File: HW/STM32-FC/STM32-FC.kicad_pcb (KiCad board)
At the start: 4 copper layers, 38 x 48 mm, 113 parts, among them J1 GH 1.25mm 6P, J10 GH 1.25mm 6P, J11 GH 1.25mm 6P, J12 GH 1.25mm 6P, J13 GH 1.25mm 4P, J14 GH 1.25mm 4P, J15 GH 1.25mm 4P, J2 USB_C_USB2.0_14P, J3 GH 1.25mm 6P, J4 Micro_SD_Card_Det1, J5 JST ZH 1.5mm 2P, J6 PWM_Conn_3x14, J7 ZH 1.5mm 3P, J8 ZH 1.5mm 4P, J9 GH 1.25mm 10P, Q1 S9013, Q2 S9013, SW2 SW_DIP_x03, U1 STM32F407VETx, U10 ATA6561-GBQW, U11 ATA6561-GBQW, U2 USBLC6-2SC6, U3 AMS1117-3.3, U4 AMS1117-3.3, U5 W25X40CLSN, U6 BMI323, U7 ICM-42688-P, U8 LIS2MDLTR, U9 LPS22HH, Y1 16MHz

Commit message: 2025.02.05 PCB routing 3
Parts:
- R17: value 10k -> 15k
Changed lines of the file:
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@@
 			)
 		)
-		(property "Value" "10k"
+		(property "Value" "15k"
 			(at 0 1.17 90)
 			(layer "F.Fab")
@@
 		(tags "Through hole pin header THT 1x03 1.27mm single row")
 		(property "Reference" "TP2"
-			(at 0 1.695 360)
+			(at 0 1.695 0)
 			(layer "B.SilkS")
 			(hide yes)
@@
 		)
 		(property "Value" "Test Pin"
-			(at 0 -4.235 360)
+			(at 0 -4.235 0)
 			(layer "B.Fab")
 			(effects
@@
 		)
 		(fp_text user "${REFERENCE}"
-			(at 1.85 0 360)
+			(at 1.85 0 0)
 			(layer "B.Fab")
 			(effects

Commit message: 2025.02.05 PCB routing done
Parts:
- removed R35: 0, Resistor_SMD:R_0402_1005Metric
- added JP1: SolderJumper_2_Open, Jumper:SolderJumper-2_P1.3mm_Open_TrianglePad1.0x1.5mm, F.Cu at (123.5, 116.4)
- moved R29 0.86 mm to (151.9, 78.9), turned to 0 degrees
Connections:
- J6 pad 2: /TIM4_CH4 -> /TIM3_CH1
- J6 pad 3: /TIM3_CH1 -> /TIM3_CH2
- J6 pad 4: /TIM3_CH2 -> /TIM4_CH4
- U1 pad 15: /RSSI_IN -> /V_BATT
- U1 pad 16: /V_BATT -> /RSSI_IN
- U1 pad 39: /GPS1_LED -> unconnected-(U1-PE8-Pad39)
- U1 pad 40: /GPS1_BUZZER -> unconnected-(U1-PE9-Pad40)
- U1 pad 41: /GPS1_LED_SW -> unconnected-(U1-PE10-Pad41)
- U1 pad 57: unconnected-(U1-PD10-Pad57) -> /GPS1_LED_SW
- U1 pad 60: unconnected-(U1-PD13-Pad60) -> /GPS1_LED
- U1 pad 65: unconnected-(U1-PC8-Pad65) -> /GPS1_BUZZER
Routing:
- net /UART5_TX: track 0.00 -> 63.7 mm, vias 0 -> 2
- net /UART5_RX: track 2.22 -> 60.2 mm, vias 0 -> 2
- net +3.3V_RC: track 10.9 -> 54.9 mm, vias 0 -> 3
- net /TIM3_CH1: track 0.00 -> 39.3 mm, vias 0 -> 1
- net /TIM3_CH2: track 0.00 -> 37.5 mm, vias 0 -> 1
- net /TIM4_CH4: track 0.00 -> 36.6 mm, vias 0 -> 1
- net /TIM1_CH4: track 17.8 -> 52.3 mm, vias 0 -> 2
- net /I2C1_SCL: track 2.22 -> 34.6 mm, vias 0 -> 2
- net /I2C1_SDA: track 3.95 -> 35.9 mm, vias 0 -> 2
- net /TIM1_CH3: track 0.00 -> 31.3 mm, vias 0 -> 2
- net /MSD_DETECT: track 0.00 -> 28.3 mm, vias 0 -> 2
- net /CAN2_STBY: track 0.00 -> 27.6 mm, vias 0 -> 3
- net /TIM1_CH2: track 0.00 -> 23.9 mm, vias 0 -> 1
- net /TIM3_CH3: track 0.00 -> 23.1 mm, vias 0 -> 1
- net /CAN1_STBY: track 0.00 -> 23.0 mm, vias 0 -> 1
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
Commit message: 2025.02.06 PCB routing done v2
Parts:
- added C35: 100nF, Capacitor_SMD:C_0402_1005Metric, F.Cu at (134.1, 97.8)
- D1, D2, D4, D5, R4, R6, R7, R8: moved to F.Cu
- moved R30 5.38 mm to (138.4, 76.4), turned to 180 degrees
- moved R26 5.00 mm to (131.0, 76.8), turned to 0 degrees
- moved R25 3.81 mm to (126.8, 100.3)
- moved R28 1.61 mm to (126.8, 97.9)
- moved R24 1.50 mm to (129.0, 77.0)
- moved R23 1.40 mm to (127.6, 77.0)
- moved R31 1.32 mm to (126.8, 99.0)
- moved R32 1.22 mm to (126.8, 100.2)
- moved R27 1.17 mm to (126.8, 99.2)
- moved D1 0.50 mm to (146.2, 104.2)
- moved D2 0.50 mm to (146.2, 101.2)
- moved D4 0.50 mm to (146.2, 102.2)
- moved D5 0.50 mm to (146.2, 103.2)
- moved R4 0.50 mm to (148.2, 104.2)
- moved R6 0.50 mm to (148.2, 101.2)
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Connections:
- J1 pad 1: +3.3V -> GND
- J1 pad 2: /SWDIO -> unconnected-(J1-Pin_2-Pad2)
- J1 pad 3: /SWCLK -> /NRST
- J1 pad 4: /NRST -> /SWCLK
- J1 pad 5: unconnected-(J1-Pin_5-Pad5) -> /SWDIO
- J1 pad 6: GND -> +3.3V
- J10 pad 1: +5V -> GND
- J10 pad 2: /UART5_TX -> /I2C2_SDA
- J10 pad 3: /UART5_RX -> /I2C2_SCL
- J10 pad 4: /I2C2_SCL -> /UART5_RX
- J10 pad 5: /I2C2_SDA -> /UART5_TX
- J10 pad 6: GND -> +5V
- J11 pad 1: +5V -> GND
- J11 pad 2: /UART2_TX -> /UART2_RTS
- J11 pad 3: /UART2_RX -> /UART2_CTS
- J11 pad 4: /UART2_CTS -> /UART2_RX
- J11 pad 5: /UART2_RTS -> /UART2_TX
- J11 pad 6: GND -> +5V
- J12 pad 1: +5V -> GND
- J12 pad 2: /UART3_TX -> /UART3_RTS
- J12 pad 3: /UART3_RX -> /UART3_CTS
- J12 pad 4: /UART3_CTS -> /UART3_RX
- J12 pad 5: /UART3_RTS -> /UART3_TX
- J12 pad 6: GND -> +5V
- J13 pad 1: +5V -> GND
- J13 pad 2: /I2C1_SCL -> /I2C1_SDA
- J13 pad 3: /I2C1_SDA -> /I2C1_SCL
- J13 pad 4: GND -> +5V
- J14 pad 1: +5V -> GND
- J14 pad 2: /Communication/CAN1_P -> /Communication/CAN1_N
- J14 pad 3: /Communication/CAN1_N -> /Communication/CAN1_P
- J14 pad 4: GND -> +5V
- J15 pad 1: +5V -> GND
- J15 pad 2: /Communication/CAN2_P -> /Communication/CAN2_N
- J15 pad 3: /Communication/CAN2_N -> /Communication/CAN2_P
- J15 pad 4: GND -> +5V
- J3 pad 1: +5V -> GND
- J3 pad 2: +5V -> GND
- J3 pad 3: /PM_CURRENT -> /PM_VOLTAGE
- J3 pad 4: /PM_VOLTAGE -> /PM_CURRENT
- J3 pad 5: GND -> +5V
- J3 pad 6: GND -> +5V
- J9 pad 1: +5V -> GND
- J9 pad 10: GND -> +5V
- J9 pad 2: /UART4_TX -> /GPS1_BUZZER
- J9 pad 3: /UART4_RX -> +3.3V
- J9 pad 4: /I2C3_SCL -> /GPS1_SW_LED
- J9 pad 5: /I2C3_SDA -> /GPS1_SW
- J9 pad 6: /GPS1_LED_SW -> /I2C3_SDA
- J9 pad 7: /GPS1_LED -> /I2C3_SCL
- J9 pad 8: +3.3V -> /UART4_RX
- J9 pad 9: /GPS1_BUZZER -> /UART4_TX
- U1 pad 37: unconnected-(U1-PB2-Pad37) -> /BOOT1
- U1 pad 57: /GPS1_LED_SW -> /GPS1_SW_LED
- U1 pad 60: /GPS1_LED -> /GPS1_SW
- U1 pad 77: /BOOT1 -> unconnected-(U1-PA15-Pad77)
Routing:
- net /GPS1_SW: track 0.00 -> 17.9 mm, vias 0 -> 2
- net /GPS1_SW_LED: track 0.00 -> 16.9 mm, vias 0 -> 2
- net +3.3V: track 113.1 -> 128.9 mm, vias 23 -> 25
- net /BOOT1: track 21.3 -> 35.5 mm
- net /GPS1_LED: track 14.1 -> 0.00 mm, vias 1 -> 0
- net /GPS1_LED_SW: track 13.5 -> 0.00 mm, vias 1 -> 0
- net /GPS1_BUZZER: track 10.7 -> 20.7 mm, vias 1 -> 2
- net /Communication/CAN1_N: track 6.02 -> 15.4 mm
- net /UART3_RX: track 22.9 -> 13.6 mm
- net /Communication/CAN1_P: track 6.02 -> 14.1 mm
- net GND: track 167.0 -> 174.4 mm, vias 26 -> 39
- net /I2C3_SDA: track 18.0 -> 24.6 mm
- net /I2C3_SCL: track 27.1 -> 20.8 mm
- net /UART4_TX: track 27.3 -> 21.3 mm
- net /UART4_RX: track 27.6 -> 21.9 mm
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
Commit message: 2025.02.06 PCB routing done v3
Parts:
- J1, J10, J11, J12, J3: footprint JST_GH:JST_GH_BM06B-GHS-TBT_06 -> JST_GH:JST_GH_SM06B-GHS-TB_06x1.25mm_Angled
- J13, J14, J15: footprint JST_GH:JST_GH_BM04B-GHS-TBT_04 -> JST_GH:JST_GH_SM04B-GHS-TB_04x1.25mm_Angled
- J9: footprint JST_GH:JST_GH_BM10B-GHS-TBT_10 -> JST_GH:JST_GH_SM10B-GHS-TB_10x1.25mm_Angled
- turned J1 to 90 degrees
- turned J10 to -90 degrees
- turned J11 to 0 degrees
- turned J12 to 0 degrees
- turned J13 to 90 degrees
- turned J14 to 180 degrees
- turned J15 to 180 degrees
- turned J3 to 0 degrees
- turned J9 to 180 degrees
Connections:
- net /TIM4_CH3 renamed /Buzzer
- J1 pad 1: GND -> +3.3V
- J1 pad 2: unconnected-(J1-Pin_2-Pad2) -> /SWDIO
- J1 pad 3: /NRST -> /SWCLK
- J1 pad 4: /SWCLK -> /NRST
- J1 pad 5: /SWDIO -> unconnected-(J1-Pin_5-Pad5)
- J1 pad 6: +3.3V -> GND
- J10 pad 1: GND -> +5V
- J10 pad 2: /I2C2_SDA -> /UART5_TX
- J10 pad 3: /I2C2_SCL -> /UART5_RX
- J10 pad 4: /UART5_RX -> /I2C2_SCL
- J10 pad 5: /UART5_TX -> /I2C2_SDA
- J10 pad 6: +5V -> GND
- J11 pad 1: GND -> +5V
- J11 pad 2: /UART2_RTS -> /UART2_TX
- J11 pad 3: /UART2_CTS -> /UART2_RX
- J11 pad 4: /UART2_RX -> /UART2_CTS
- J11 pad 5: /UART2_TX -> /UART2_RTS
- J11 pad 6: +5V -> GND
- J12 pad 1: GND -> +5V
- J12 pad 2: /UART3_RTS -> /UART3_TX
- J12 pad 3: /UART3_CTS -> /UART3_RX
- J12 pad 4: /UART3_RX -> /UART3_CTS
- J12 pad 5: /UART3_TX -> /UART3_RTS
- J12 pad 6: +5V -> GND
- J13 pad 1: GND -> +5V
- J13 pad 2: /I2C1_SDA -> /I2C1_SCL
- J13 pad 3: /I2C1_SCL -> /I2C1_SDA
- J13 pad 4: +5V -> GND
- J14 pad 1: GND -> +5V
- J14 pad 2: /Communication/CAN1_N -> /Communication/CAN1_P
- J14 pad 3: /Communication/CAN1_P -> /Communication/CAN1_N
- J14 pad 4: +5V -> GND
- J15 pad 1: GND -> +5V
- J15 pad 2: /Communication/CAN2_N -> /Communication/CAN2_P
- J15 pad 3: /Communication/CAN2_P -> /Communication/CAN2_N
- J15 pad 4: +5V -> GND
- J3 pad 1: GND -> +5V
- J3 pad 2: GND -> +5V
- J3 pad 3: /PM_VOLTAGE -> /PM_CURRENT
- J3 pad 4: /PM_CURRENT -> /PM_VOLTAGE
- J3 pad 5: +5V -> GND
- J3 pad 6: +5V -> GND
- J9 pad 1: GND -> +5V
- J9 pad 10: +5V -> GND
- J9 pad 2: /GPS1_BUZZER -> /UART4_TX
- J9 pad 3: +3.3V -> /UART4_RX
- J9 pad 4: /GPS1_SW_LED -> /I2C3_SCL
- J9 pad 5: /GPS1_SW -> /I2C3_SDA
- J9 pad 6: /I2C3_SDA -> /GPS1_SW
- J9 pad 7: /I2C3_SCL -> /GPS1_SW_LED
- J9 pad 8: /UART4_RX -> +3.3V
- J9 pad 9: /UART4_TX -> /GPS1_BUZZER
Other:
- board size 38 x 48 mm -> 39 x 48.5 mm

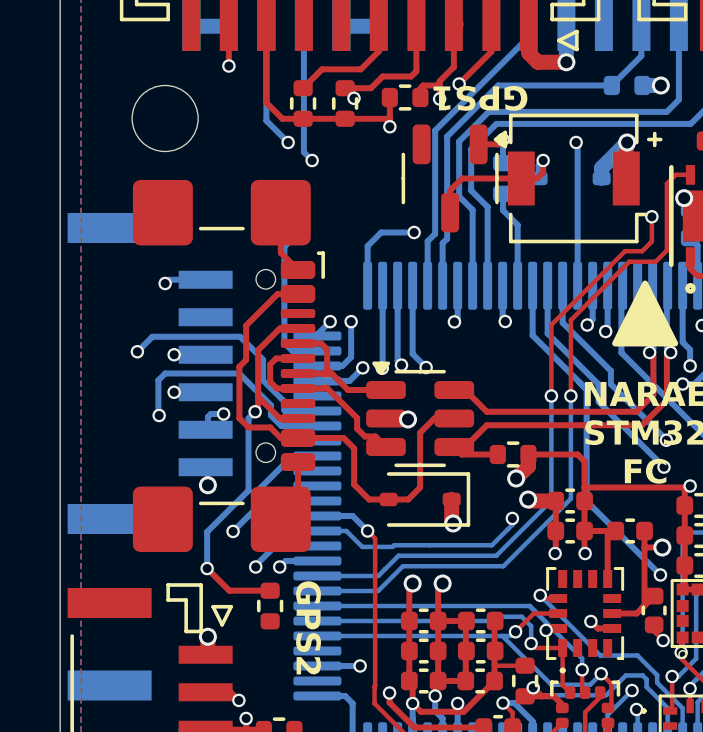
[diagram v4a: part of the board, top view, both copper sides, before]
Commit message: 2025.02.07 USB C Conn change v1
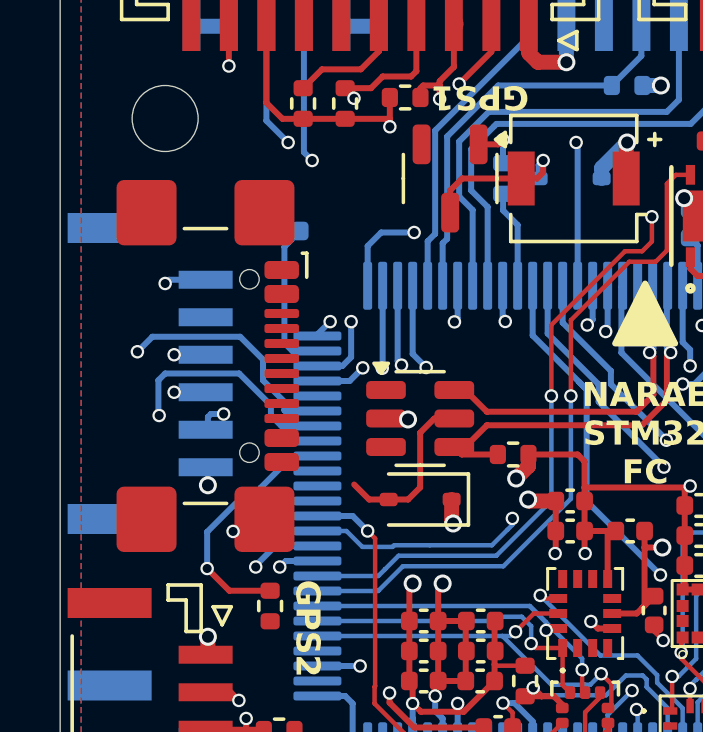
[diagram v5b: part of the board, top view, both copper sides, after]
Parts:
- C22: value 0.1nF -> 100pF
- C26: value 4.7u -> 4.7uF
- D4: value Green -> Yellow
- J2: footprint Connector_USB:USB_C_Receptacle_GCT_USB4110 -> USB_C:918-418K2023S40023
- U5: value W25X40CLSN -> W25X40CLUXIG
- moved J2 0.55 mm to (123.2, 85.8)
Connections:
- net /LED_GREEN renamed /LED_YELLOW
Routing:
- net VBUS: track 16.5 -> 5.73 mm
- net Net-(J2-CC1): track 13.7 -> 5.58 mm, vias 2 -> 1
- net /USB & POWER/USB_CONN_D+: track 6.58 -> 0.00 mm
- net /USB & POWER/USB_CONN_D-: track 5.11 -> 0.00 mm
- net GND: track 174.4 -> 170.1 mm

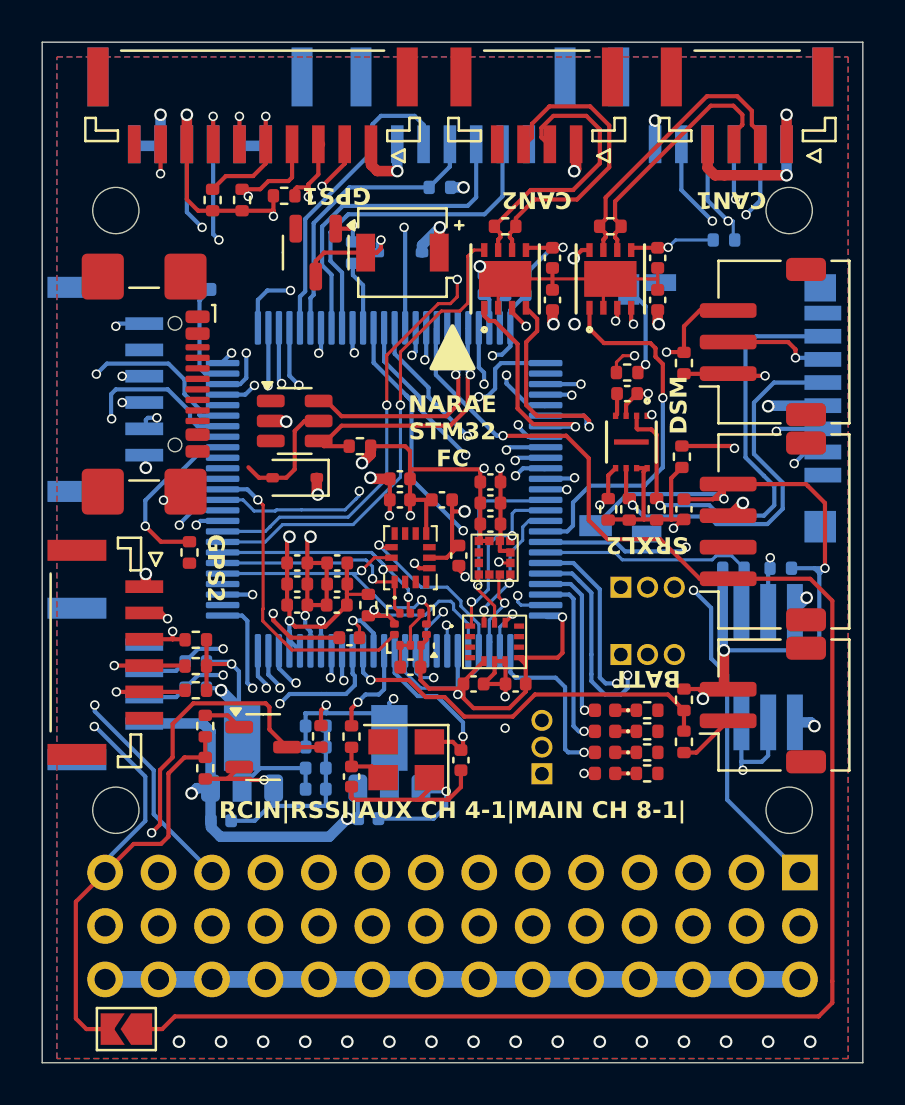
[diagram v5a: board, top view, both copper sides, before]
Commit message: 2025.02.07 USB C Conn chage v2
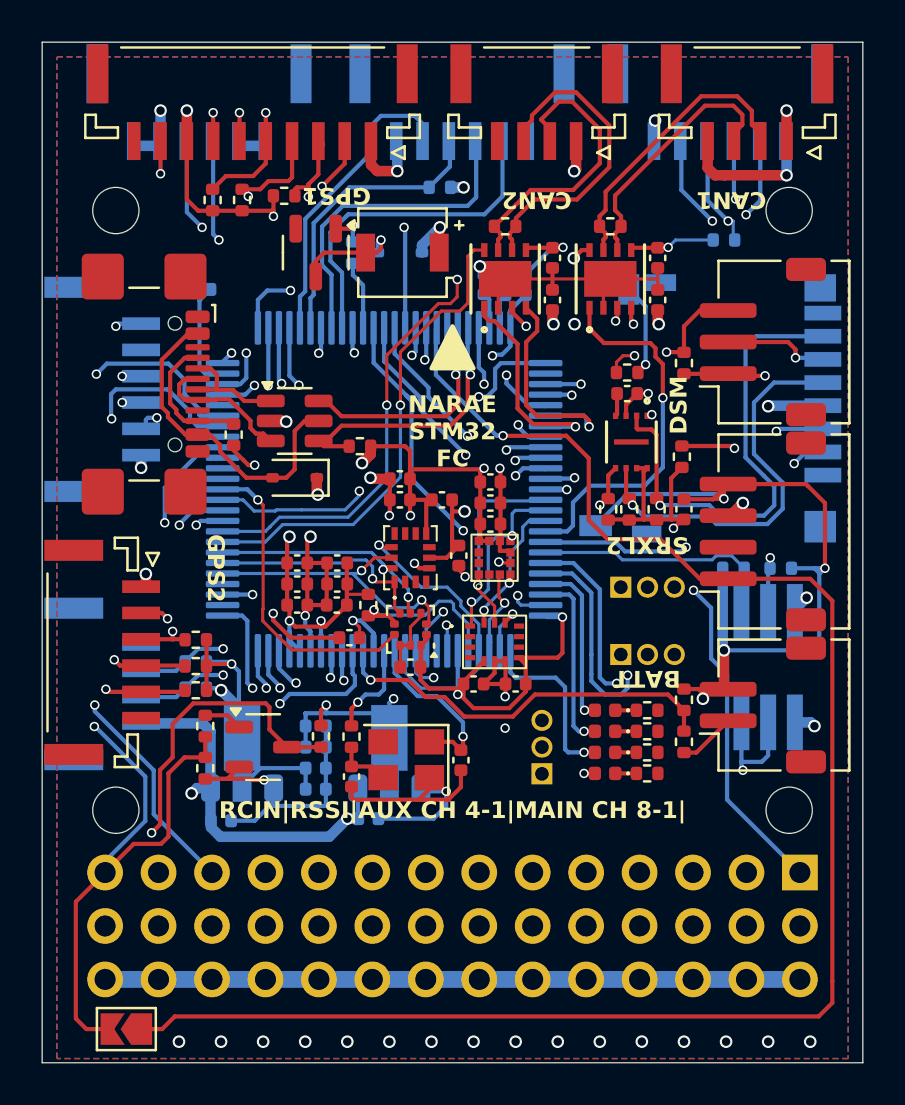
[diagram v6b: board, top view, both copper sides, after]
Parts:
- moved R9 5.98 mm to (128.6, 88.2)
- moved J11 0.16 mm to (151.7, 72.6)
- moved J12 0.16 mm to (139.4, 72.6)
- moved J3 0.16 mm to (127.0, 72.6)
- moved J1 0.15 mm to (122.6, 86.0)
- moved J10 0.15 mm to (122.6, 98.5)
- moved J13 0.15 mm to (122.6, 100.0)
- moved J14 0.15 mm to (143.0, 72.6)
- moved J15 0.15 mm to (153.0, 72.6)
- moved J9 0.15 mm to (129.5, 72.6)
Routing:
- net VBUS: track 5.73 -> 15.8 mm
- net /USB & POWER/USB_CONN_D+: track 0.00 -> 6.95 mm
- net /USB & POWER/USB_CONN_D-: track 0.00 -> 5.46 mm
- net GND: track 170.1 -> 171.6 mm, vias 39 -> 40
- net /Communication/CAN2_N: track 13.0 -> 12.0 mm
- net Net-(J2-CC1): track 5.58 -> 6.58 mm, vias 1 -> 0
